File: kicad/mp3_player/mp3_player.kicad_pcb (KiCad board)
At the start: 2 copper layers, 78.7 x 61 mm, 15 parts, among them J1 ESP8266-left, J2 ESP8266-right, J3 AC 220, J4 player-left, J5 player-right, J6 Conn_01x02_Socket, J7 Conn_01x02_Socket, SW1 SW_Push, U2 LF15_TO220

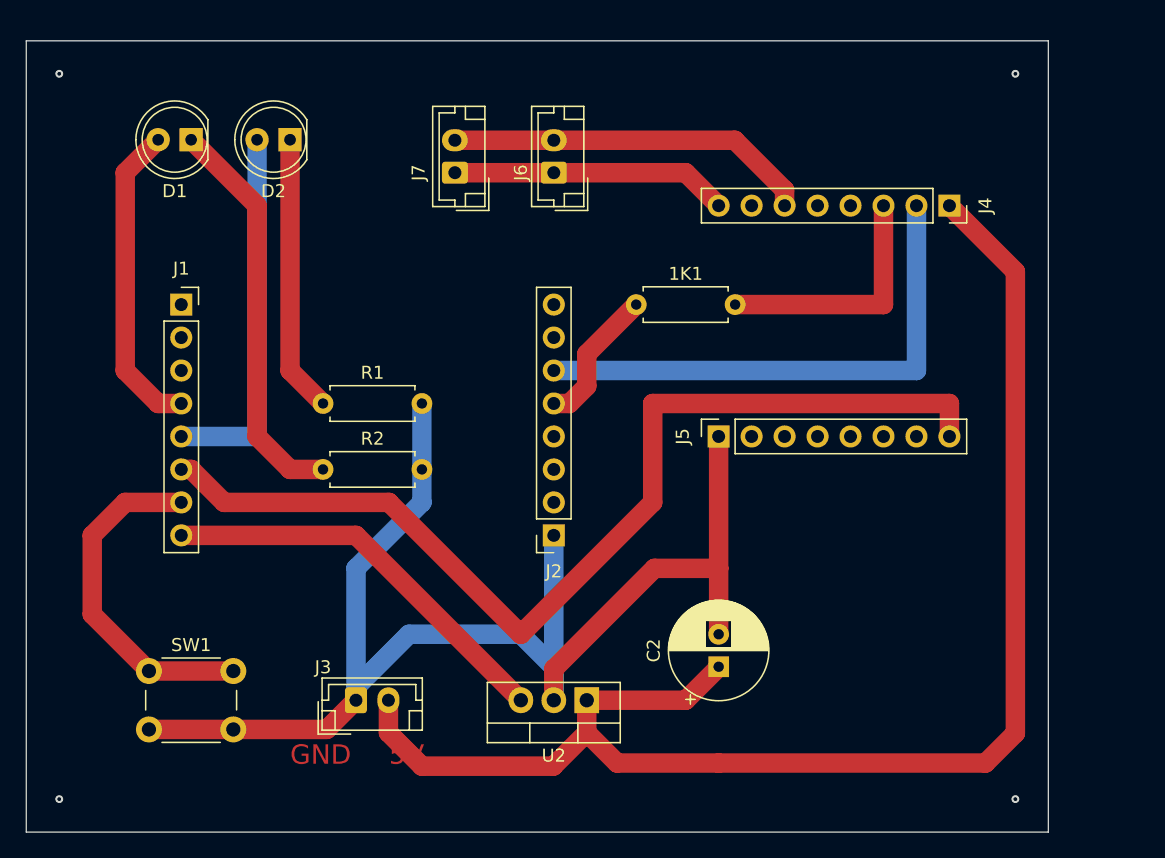
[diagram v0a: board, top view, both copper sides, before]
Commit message: wifimanager only needs to be started once
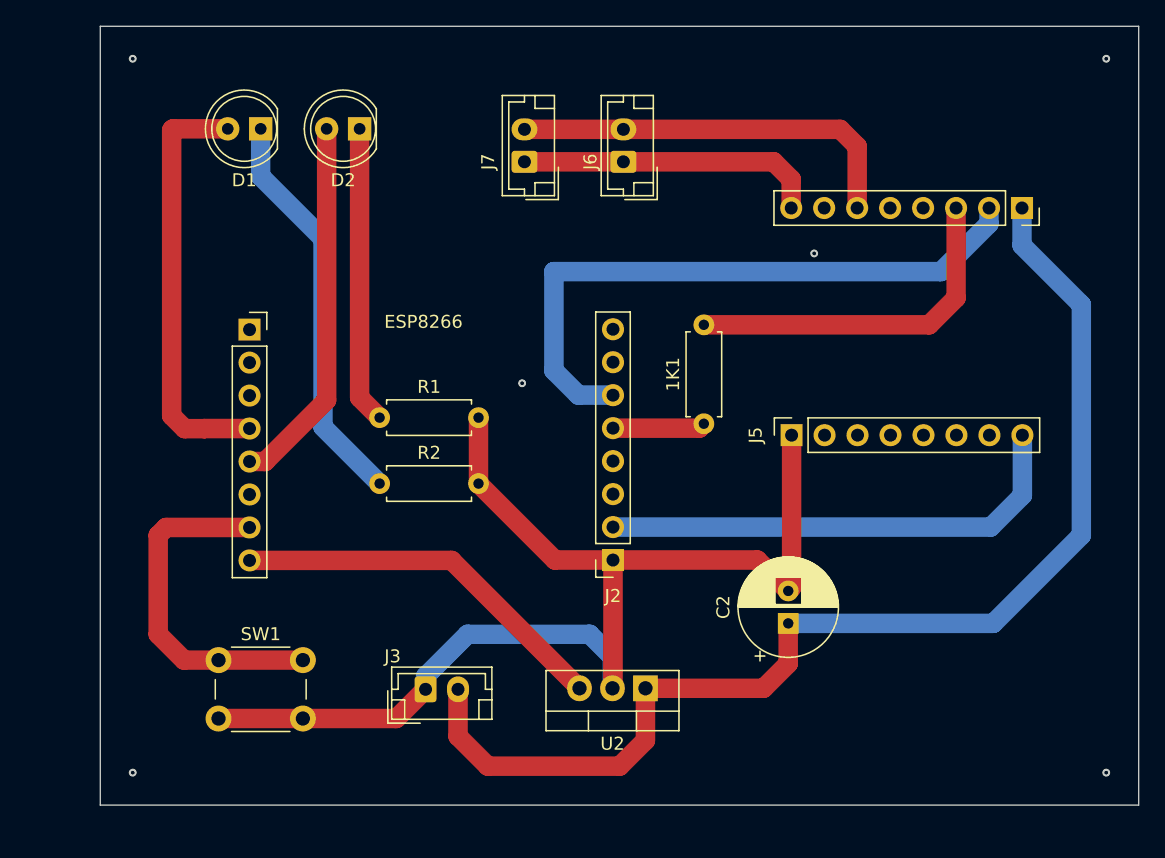
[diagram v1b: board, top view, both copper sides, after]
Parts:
- SW1: footprint Button_Switch_THT:SW_PUSH_6mm -> Button_Switch_THT:SW_PUSH_6mm_H4.3mm
- moved 1K1 10.6 mm to (166.5, 100.6), turned to 90 degrees
- moved C2 6.32 mm to (173.0, 116.0)
- moved J5 5.62 mm to (173.3, 101.5)
- moved ESP8266 5.60 mm to (131.5, 93.4)
- moved Player 5.59 mm to (191.0, 84.0)
- moved J3 5.43 mm to (145.1, 121.1)
- moved J6 5.43 mm to (160.3, 80.4)
- moved J7 5.43 mm to (152.7, 80.4)
- moved SW1 5.43 mm to (129.1, 118.8)
- moved D1 5.43 mm to (132.4, 77.9)
- moved D2 5.43 mm to (140.0, 77.9)
- moved J2 4.94 mm to (159.5, 111.1)
- moved U2 4.61 mm to (162.0, 121.0)
- moved R1 4.49 mm to (141.5, 100.2)
- moved R2 4.49 mm to (141.5, 105.2)
- renumbered J1 to ESP8266, J4 to Player
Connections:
- ESP8266 pad 6: BUSY -> unconnected-(J1-Pin_6-Pad6)
- J2 pad 2: unconnected-(J2-Pin_2-Pad2) -> BUSY
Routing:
- net BUSY: track 78.8 -> 37.2 mm
- net 5V: track 111.4 -> 91.2 mm
- net GND: track 109.6 -> 91.1 mm
- net TX: track 40.6 -> 49.2 mm
- net Net-(D1-A): track 24.2 -> 32.8 mm
- net RX: track 19.1 -> 27.2 mm
- net Net-(J2-Pin_5): track 11.0 -> 7.14 mm
- net Net-(J4-Pin_6): track 28.2 -> 30.9 mm
- net Net-(J4-Pin_8): track 21.4 -> 23.3 mm
- net 3.3V: track 31.4 -> 29.5 mm
- net Net-(D2-K): track 21.4 -> 22.9 mm
- net (no net): vias 4 -> 6
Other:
- board size 78.7 x 61 mm -> 80 x 60 mm
- board text removed: "5V"
- board text removed: "GND"

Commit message: many changes. Main workaround to loop on faulty player
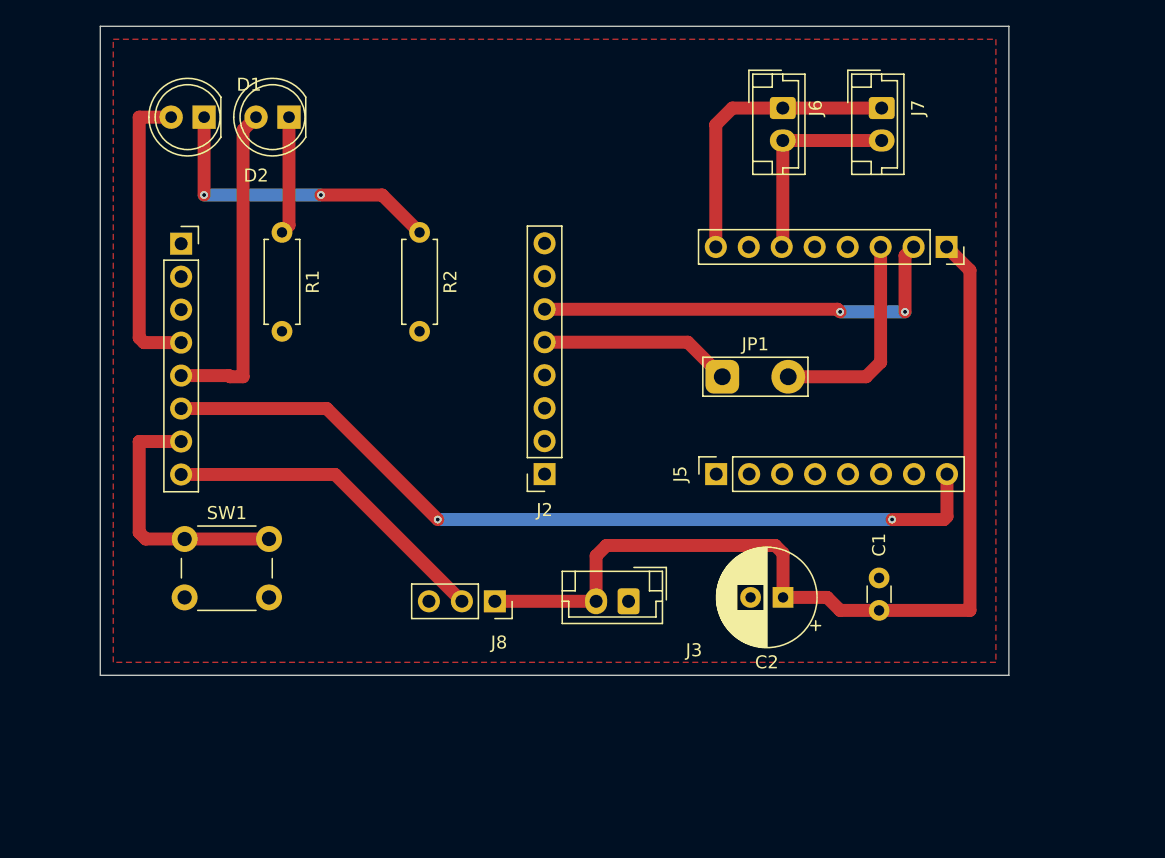
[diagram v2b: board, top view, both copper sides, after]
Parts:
- removed 1K1: R, Resistor_THT:R_Axial_DIN0207_L6.3mm_D2.5mm_P7.62mm_Horizontal
- removed U2: LF15_TO220, Package_TO_SOT_THT:TO-220-3_Vertical
- added C1: C, Capacitor_THT:C_Disc_D3.0mm_W1.6mm_P2.50mm, F.Cu at (180.0, 115.0)
- added J8: Conn_01x03_Socket, Connector_PinSocket_2.54mm:PinSocket_1x03_P2.54mm_Vertical, F.Cu at (150.4, 114.3)
- added JP1: Jumper_2_Open, TestPoint:TestPoint_2Pads_Pitch5.08mm_Drill1.3mm, F.Cu at (167.9, 97.0)
- moved J7 27.8 mm to (180.2, 76.3), turned to -90 degrees
- moved R2 19.6 mm to (144.6, 85.9), turned to -90 degrees
- moved J3 17.0 mm to (160.7, 114.3), turned to 180 degrees
- moved R1 16.1 mm to (134.0, 85.9), turned to -90 degrees
- moved J6 13.0 mm to (172.6, 76.3), turned to -90 degrees
- moved SW1 9.69 mm to (126.5, 109.5)
- moved J2 8.46 mm to (154.2, 104.5)
- moved J1 8.46 mm to (126.2, 86.8)
- moved J4 6.54 mm to (185.2, 87.0)
- moved J5 6.54 mm to (167.4, 104.5)
- moved D2 5.51 mm to (134.5, 77.0)
- moved D1 4.45 mm to (128.0, 77.0)
- moved C2 2.04 mm to (172.6, 114.0), turned to 180 degrees
- renumbered ESP8266 to J1, Player to J4
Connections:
- J1 pad 6: unconnected-(J1-Pin_6-Pad6) -> BUSY
- J2 pad 2: BUSY -> unconnected-(J2-Pin_2-Pad2)
- J5 pad 1: GND -> unconnected-(J5-Pin_1-Pad1)
- J5 pad 2: unconnected-(J5-Pin_2-Pad2) -> GND
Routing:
- net GND: track 91.1 -> 0.00 mm
- net BUSY: track 37.2 -> 65.9 mm, vias 0 -> 2
- net 5V: track 91.2 -> 73.2 mm
- net TX: track 49.2 -> 33.1 mm, vias 0 -> 2
- net Net-(J4-Pin_6): track 30.9 -> 15.9 mm
- net Net-(D2-K): track 22.9 -> 9.10 mm
- net RX: track 27.2 -> 16.5 mm
- net Net-(D1-A): track 32.8 -> 22.8 mm
- net Net-(J2-Pin_5): track 7.14 -> 14.8 mm
- net Net-(D1-K): track 31.1 -> 23.8 mm, vias 0 -> 2
- net RESET: track 26.9 -> 20.4 mm
- net 3.3V: track 29.5 -> 25.7 mm
- net Net-(D2-A): track 28.8 -> 25.2 mm
- net Net-(J4-Pin_8): track 23.3 -> 22.7 mm
- net (no net): vias 6 -> 0
- added copper zone on F.Cu, net GND
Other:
- board size 80 x 60 mm -> 70 x 50 mm

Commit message: wip board with ground plane
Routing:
- net 5V: track 73.2 -> 51.4 mm
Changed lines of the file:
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@@
-	)
-	(segment
-		(start 172.6 110.6)
-		(end 172.6 114)
-		(width 1)
-		(layer "F.Cu")
-		(net 3)
-	)
-	(segment
-		(start 158.2 114.3)
-		(end 158.2 110.8)
-		(width 1)
-		(layer "F.Cu")
-		(net 3)
 	)
 	(segment
@@
 	)
 	(segment
-		(start 158.2 110.8)
-		(end 159 110)
-		(width 1)
-		(layer "F.Cu")
-		(net 3)
-	)
-	(segment
 		(start 150.4 114.3)
 		(end 158.2 114.3)
@@
 		(width 1)
 		(layer "F.Cu")
-		(net 3)
-	)
-	(segment
-		(start 159 110)
-		(end 172 110)
-		(width 1)
-		(layer "F.Cu")
-		(net 3)
-	)
-	(segment
-		(start 172 110)
-		(end 172.6 110.6)
-		(width 1)
-		(layer "F.Cu")
